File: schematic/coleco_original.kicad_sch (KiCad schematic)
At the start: 6 parts

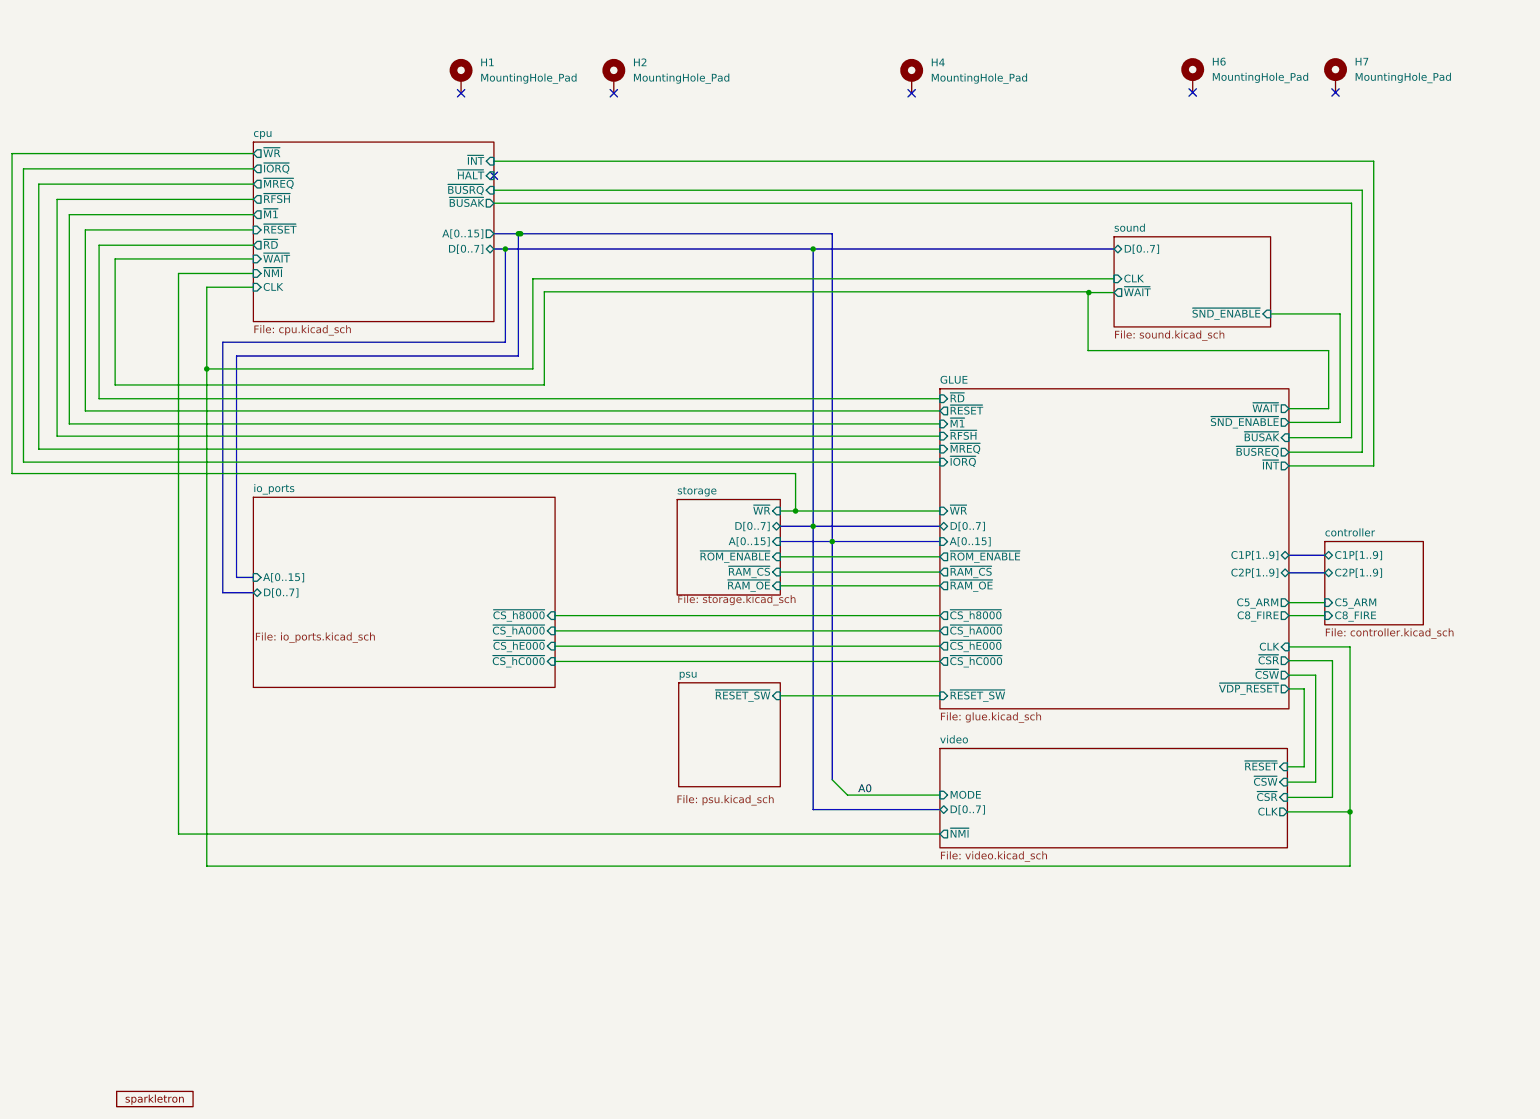
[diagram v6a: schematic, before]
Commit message: first commit with PCB revised for super game module. Needs model updates and tweaks
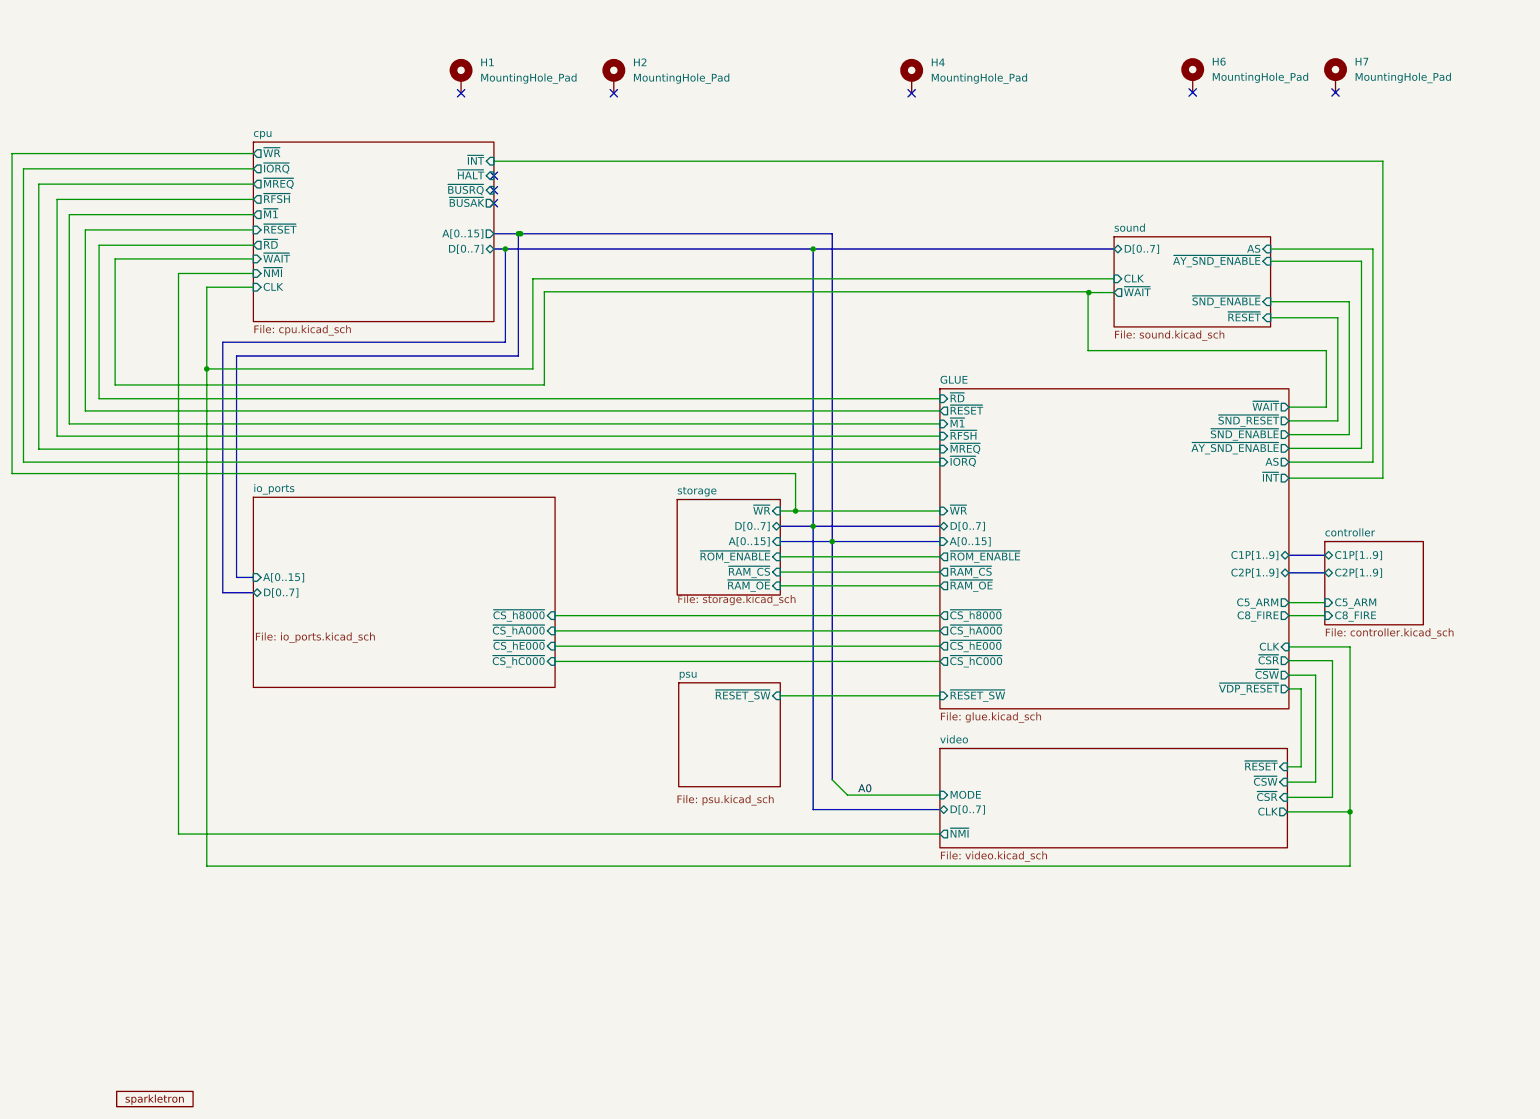
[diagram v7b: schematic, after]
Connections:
- no-connect marks 6 -> 8
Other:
- sheet GLUE ports: added AS, ~{AY_SND_ENABLE}, ~{SND_RESET}; removed ~{BUSAK}, ~{BUSREQ}
- sheet sound ports: added AS, ~{AY_SND_ENABLE}, ~{RESET}; removed none
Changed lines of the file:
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@@
   (no_connect (at 216.408 32.004))
   (no_connect (at 120.142 32.131))
+  (no_connect (at 100.203 50.419))
   (no_connect (at 100.203 45.847))
   (no_connect (at 240.157 32.004))
+  (no_connect (at 100.203 48.26))
   (no_connect (at 94.742 32.131))
   (no_connect (at 169.672 32.131))
@@
     (stroke (width 0) (type default))
   )
+  (wire (pts (xy 246.38 93.472) (xy 246.38 58.039))
+    (stroke (width 0) (type default))
+  )
   (wire (pts (xy 242.57 124.206) (xy 242.57 151.638))
     (stroke (width 0) (type default))
@@
     (stroke (width 0) (type default))
   )
-  (wire (pts (xy 244.602 91.821) (xy 244.602 48.26))
+  (wire (pts (xy 240.538 86.614) (xy 240.538 69.469))
     (stroke (width 0) (type default))
   )
@@
     (stroke (width 0) (type default))
   )
-  (wire (pts (xy 100.203 43.434) (xy 246.507 43.434))
+  (wire (pts (xy 232.41 86.614) (xy 240.538 86.614))
+    (stroke (width 0) (type default))
+  )
+  (wire (pts (xy 100.203 43.434) (xy 248.031 43.434))
     (stroke (width 0) (type default))
   )
@@
     (stroke (width 0) (type default))
   )
-  (wire (pts (xy 246.507 43.434) (xy 246.507 94.107))
+  (wire (pts (xy 248.031 43.434) (xy 248.031 96.139))
     (stroke (width 0) (type default))
   )
@@
     (stroke (width 0) (type default))
   )
-  (wire (pts (xy 234.95 131.191) (xy 234.95 144.145))
+  (wire (pts (xy 234.442 131.191) (xy 234.442 144.145))
     (stroke (width 0) (type default))
   )
@@
     (stroke (width 0) (type default))
   )
-  (wire (pts (xy 232.156 144.145) (xy 234.95 144.145))
+  (wire (pts (xy 232.156 144.145) (xy 234.442 144.145))
+    (stroke (width 0) (type default))
+  )
+  (wire (pts (xy 232.41 93.472) (xy 246.38 93.472))
     (stroke (width 0) (type default))
   )
@@
     (stroke (width 0) (type default))
   )
-  (wire (pts (xy 100.203 50.419) (xy 242.824 50.419))
-    (stroke (width 0) (type default))
-  )
   (bus (pts (xy 55.118 73.533) (xy 55.118 115.189))
     (stroke (width 0) (type default))
@@
     (stroke (width 0) (type default))
   )
-  (wire (pts (xy 232.41 91.821) (xy 244.602 91.821))
+  (wire (pts (xy 246.38 58.039) (xy 229.362 58.039))
     (stroke (width 0) (type default))
   )
@@
     (stroke (width 0) (type default))
   )
-  (wire (pts (xy 232.41 131.191) (xy 234.95 131.191))
+  (wire (pts (xy 232.41 131.191) (xy 234.442 131.191))
     (stroke (width 0) (type default))
   )
@@
     (stroke (width 0) (type default))
   )
+  (wire (pts (xy 244.475 60.071) (xy 229.362 60.071))
+    (stroke (width 0) (type default))
+  )
   (wire (pts (xy 232.41 118.999) (xy 238.379 118.999))
     (stroke (width 0) (type default))
@@
     (stroke (width 0) (type default))
   )
-  (wire (pts (xy 240.919 68.834) (xy 229.362 68.834))
+  (wire (pts (xy 242.443 66.802) (xy 229.362 66.802))
     (stroke (width 0) (type default))
   )
@@
     (stroke (width 0) (type default))
   )
-  (wire (pts (xy 232.41 84.582) (xy 239.014 84.582))
+  (wire (pts (xy 232.41 84.328) (xy 238.633 84.328))
     (stroke (width 0) (type default))
   )
@@
     (stroke (width 0) (type default))
   )
-  (wire (pts (xy 242.824 50.419) (xy 242.824 89.408))
-    (stroke (width 0) (type default))
-  )
-  (wire (pts (xy 239.014 74.93) (xy 199.009 74.93))
+  (wire (pts (xy 238.633 74.93) (xy 199.009 74.93))
     (stroke (width 0) (type default))
   )
@@
     (stroke (width 0) (type default))
   )
+  (wire (pts (xy 229.362 69.469) (xy 240.538 69.469))
+    (stroke (width 0) (type default))
+  )
   (wire (pts (xy 108.585 65.151) (xy 108.585 80.645))
     (stroke (width 0) (type default))
@@
     (stroke (width 0) (type default))
   )
-  (wire (pts (xy 232.41 86.868) (xy 240.919 86.868))
+  (wire (pts (xy 232.41 88.9) (xy 242.443 88.9))
     (stroke (width 0) (type default))
   )
@@
     (stroke (width 0) (type default))
   )
-  (wire (pts (xy 246.507 94.107) (xy 232.41 94.107))
+  (wire (pts (xy 248.031 96.139) (xy 232.41 96.139))
     (stroke (width 0) (type default))
   )
@@
     (stroke (width 0) (type default))
   )
+  (wire (pts (xy 244.475 91.186) (xy 244.475 60.071))
+    (stroke (width 0) (type default))
+  )
   (bus (pts (xy 104.267 55.499) (xy 104.648 55.499))
     (stroke (width 0) (type default))
@@
     (stroke (width 0) (type default))
   )
-  (wire (pts (xy 242.824 89.408) (xy 232.41 89.408))
-    (stroke (width 0) (type default))
-  )
   (bus (pts (xy 55.118 115.189) (xy 60.198 115.189))
     (stroke (width 0) (type default))
@@
     (stroke (width 0) (type default))
   )
-  (wire (pts (xy 240.919 86.868) (xy 240.919 68.834))
+  (wire (pts (xy 242.443 88.9) (xy 242.443 66.802))
     (stroke (width 0) (type default))
   )
@@
     (stroke (width 0) (type default))
   )
-  (wire (pts (xy 244.602 48.26) (xy 100.203 48.26))
-    (stroke (width 0) (type default))
-  )
   (bus (pts (xy 232.41 111.887) (xy 238.379 111.887))
     (stroke (width 0) (type default))
@@
     (stroke (width 0) (type default))
   )
-  (wire (pts (xy 239.014 84.582) (xy 239.014 74.93))
+  (wire (pts (xy 232.41 91.186) (xy 244.475 91.186))
+    (stroke (width 0) (type default))
+  )
+  (wire (pts (xy 238.633 84.328) (xy 238.633 74.93))
     (stroke (width 0) (type default))
   )
@@
       (effects (font (size 1.27 1.27)) (justify left))
     )
-    (pin "~{SND_ENABLE}" input (at 229.362 68.834 0)
+    (pin "~{SND_ENABLE}" input (at 229.362 66.802 0)
       (effects (font (size 1.27 1.27)) (justify right))
     )
     (pin "CLK" input (at 203.327 62.992 180)
       (effects (font (size 1.27 1.27)) (justify left))
+    )
+    (pin "~{RESET}" input (at 229.362 69.469 0)
+      (effects (font (size 1.27 1.27)) (justify right))
+    )
+    (pin "~{AY_SND_ENABLE}" input (at 229.362 60.071 0)
+      (effects (font (size 1.27 1.27)) (justify right))
+    )
+    (pin "AS" input (at 229.362 58.039 0)
+      (effects (font (size 1.27 1.27)) (justify right))
     )
     (instances
@@
       (effects (font (size 1.27 1.27)) (justify left))
     )
-    (pin "~{SND_ENABLE}" output (at 232.41 86.868 0)
+    (pin "~{SND_ENABLE}" output (at 232.41 88.9 0)
       (effects (font (size 1.27 1.27)) (justify right))
     )
@@
       (effects (font (size 1.27 1.27)) (justify right))
     )
-    (pin "~{WAIT}" output (at 232.41 84.582 0)
+    (pin "~{WAIT}" output (at 232.41 84.328 0)
       (effects (font (size 1.27 1.27)) (justify right))
     )
@@
       (effects (font (size 1.27 1.27)) (justify left))
     )
-    (pin "~{INT}" output (at 232.41 94.107 0)
+    (pin "~{INT}" output (at 232.41 96.139 0)
       (effects (font (size 1.27 1.27)) (justify right))
     )
@@
       (effects (font (size 1.27 1.27)) (justify left))
     )
-    (pin "~{BUSREQ}" output (at 232.41 91.821 0)
-      (effects (font (size 1.27 1.27)) (justify right))
-    )
-    (pin "~{BUSAK}" input (at 232.41 89.408 0)
-      (effects (font (size 1.27 1.27)) (justify right))
-    )
     (pin "C8_FIRE" output (at 232.41 118.999 0)
       (effects (font (size 1.27 1.27)) (justify right))
@@
       (effects (font (size 1.27 1.27)) (justify right))
     )
+    (pin "~{SND_RESET}" output (at 232.41 86.614 0)
+      (effects (font (size 1.27 1.27)) (justify right))
+    )
+    (pin "~{AY_SND_ENABLE}" output (at 232.41 91.186 0)
+      (effects (font (size 1.27 1.27)) (justify right))
+    )
+    (pin "AS" output (at 232.41 93.472 0)
+      (effects (font (size 1.27 1.27)) (justify right))
+    )
